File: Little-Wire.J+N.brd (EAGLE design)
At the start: 65 x 20 mm, 19 parts, among them J1 AVR_SPI_PRG_6PTH, J2 DCJ0202, X1 USB-A-H

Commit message: fixed stuff
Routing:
- net GND: track 14.2 -> 39.0 mm, vias 2 -> 1
- net VCC_HEADER: track 22.1 -> 11.1 mm
- net PIN4: track 27.2 -> 21.0 mm
- net PIN1: track 22.7 -> 24.1 mm
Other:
- board size 65 x 20 mm -> 65 x 22 mm
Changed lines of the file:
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@@
 <setting verticaltext="up"/>
 </settings>
-<grid distance="7" unitdist="mil" unit="mil" style="lines" multiple="1" display="yes" altdistance="0.025" altunitdist="inch" altunit="inch"/>
+<grid distance="0.5" unitdist="mm" unit="mm" style="lines" multiple="1" display="yes" altdistance="0.025" altunitdist="inch" altunit="inch"/>
 <layers>
 <layer number="1" name="Top" color="4" fill="1" visible="yes" active="yes"/>
@@
 <board>
 <plain>
-<wire x1="0" y1="0" x2="65" y2="0" width="0" layer="20"/>
-<wire x1="65" y1="0" x2="65" y2="20" width="0" layer="20"/>
+<wire x1="0" y1="-2" x2="65" y2="-2" width="0" layer="20"/>
+<wire x1="65" y1="-2" x2="65" y2="20" width="0" layer="20"/>
 <wire x1="65" y1="20" x2="0" y2="20" width="0" layer="20"/>
-<wire x1="0" y1="20" x2="0" y2="0" width="0" layer="20"/>
+<wire x1="0" y1="20" x2="0" y2="-2" width="0" layer="20"/>
 </plain>
 <attributes>
@@
 <autorouter>
 <pass name="Default">
-<param name="RoutingGrid" value="7mil"/>
+<param name="RoutingGrid" value="0.05mm"/>
 <param name="tpViaShape" value="round"/>
 <param name="PrefDir.1" value="|"/>
@@
 <contactref element="J2" pad="2"/>
 <contactref element="T2" pad="3"/>
-<polygon width="1.27" layer="16" isolate="0.3048" orphans="yes">
-<vertex x="0" y="19.9136"/>
-<vertex x="64.897" y="19.9136"/>
-<vertex x="64.897" y="0"/>
-<vertex x="0" y="0"/>
-</polygon>
-<polygon width="1.27" layer="1" isolate="0.3048" orphans="yes">
-<vertex x="0" y="19.9136"/>
-<vertex x="64.897" y="19.9136"/>
-<vertex x="64.897" y="0"/>
-<vertex x="0" y="0"/>
-</polygon>
 <wire x1="7.2898" y1="15.2908" x2="5.5118" y2="13.5128" width="0.254" layer="1"/>
 <wire x1="7.2898" y1="17.9578" x2="7.2898" y2="15.2908" width="0.254" layer="1"/>
 <wire x1="5.5118" y1="13.5128" x2="5.4" y2="13.5" width="0.254" layer="1"/>
 <wire x1="7.2898" y1="17.9578" x2="7.46" y2="18" width="0.254" layer="1"/>
-<wire x1="49.9618" y1="16.5354" x2="49.66485" y2="15.990384375" width="0.254" layer="1"/>
-<wire x1="47.2948" y1="17.0688" x2="47.539528125" y2="17.1811125" width="0.254" layer="1"/>
-<wire x1="52.0954" y1="17.0688" x2="52.539528125" y2="17.1811125" width="0.254" layer="1"/>
-<wire x1="46.9392" y1="17.2466" x2="47.539528125" y2="17.1811125" width="0.254" layer="1"/>
-<via x="52.451" y="17.4244" extent="1-16" drill="0.6096"/>
-<wire x1="40.7162" y1="11.3792" x2="39.4716" y2="11.3792" width="0.254" layer="1"/>
-<wire x1="39.4716" y1="11.3792" x2="39.3114" y2="11.4012" width="0.254" layer="1"/>
-<wire x1="40.7162" y1="11.3792" x2="40.3998" y2="11.831296875" width="0.254" layer="16"/>
-<wire x1="54.4068" y1="9.779" x2="54.4068" y2="9.3000125" width="0.254" layer="16"/>
-<wire x1="55.2958" y1="9.779" x2="55.2958" y2="9.29998125" width="0.254" layer="16"/>
-<wire x1="53.1622" y1="10.8458" x2="53.376184375" y2="11.188996875" width="0.254" layer="16"/>
-<wire x1="56.7182" y1="9.779" x2="56.7182" y2="9.29998125" width="0.254" layer="16"/>
-<via x="40.7162" y="11.3792" extent="1-16" drill="0.6096"/>
-<wire x1="55.8292" y1="9.6012" x2="55.8292" y2="9.29998125" width="0.254" layer="16"/>
-<wire x1="57.0738" y1="9.2456" x2="57.2925875" y2="8.691496875" width="0.254" layer="16"/>
-<wire x1="52.0954" y1="10.3124" x2="52.251821875" y2="10.723271875" width="0.254" layer="16"/>
-<wire x1="56.3626" y1="10.668" x2="56.923271875" y2="10.548175" width="0.254" layer="16"/>
-<wire x1="56.7182" y1="8.001" x2="56.337275" y2="7.602171875" width="0.254" layer="16"/>
-<wire x1="56.5404" y1="10.3124" x2="57.0740125" y2="10.351721875" width="0.254" layer="16"/>
-<wire x1="39.3114" y1="11.4012" x2="31.54" y2="12.92" width="0" layer="19" extent="1-1"/>
-<wire x1="23.19" y1="2.19" x2="31.54" y2="12.92" width="0" layer="19" extent="1-1"/>
-<wire x1="20" y1="2.46" x2="23.19" y2="2.19" width="0" layer="19" extent="1-1"/>
+<wire x1="20" y1="2.46" x2="23.19" y2="2.46" width="0.4064" layer="16"/>
+<wire x1="23.19" y1="2.46" x2="23.19" y2="2.19" width="0.4064" layer="16"/>
+<wire x1="23.19" y1="2.46" x2="27.559" y2="2.4892" width="0.254" layer="16"/>
+<wire x1="27.559" y1="2.4892" x2="27.559" y2="5.8674" width="0.254" layer="16"/>
+<wire x1="27.559" y1="5.8674" x2="32.1818" y2="5.8674" width="0.254" layer="16"/>
+<wire x1="32.1818" y1="5.8674" x2="32.1818" y2="10.8458" width="0.254" layer="16"/>
+<wire x1="32.1818" y1="10.8458" x2="31.54" y2="12.92" width="0.254" layer="16"/>
+<wire x1="38.4048" y1="12.446" x2="39.2938" y2="11.557" width="0.254" layer="1"/>
+<wire x1="38.4048" y1="13.335" x2="38.4048" y2="12.446" width="0.254" layer="1"/>
+<wire x1="36.9824" y1="14.7574" x2="38.4048" y2="13.335" width="0.254" layer="16"/>
+<wire x1="33.4264" y1="14.7574" x2="36.9824" y2="14.7574" width="0.254" layer="16"/>
+<wire x1="31.6484" y1="12.9794" x2="33.4264" y2="14.7574" width="0.254" layer="16"/>
+<wire x1="39.2938" y1="11.557" x2="39.3114" y2="11.4012" width="0.254" layer="1"/>
+<wire x1="31.6484" y1="12.9794" x2="31.54" y2="12.92" width="0.254" layer="16"/>
+<via x="38.4048" y="13.335" extent="1-16" drill="0.6096"/>
+<polygon width="0" layer="1" isolate="0.4064" orphans="yes">
+<vertex x="0" y="20"/>
+<vertex x="65" y="20"/>
+<vertex x="65" y="-2"/>
+<vertex x="0" y="-2"/>
+</polygon>
+<polygon width="0" layer="16" isolate="0.4064" orphans="yes">
+<vertex x="0" y="20"/>
+<vertex x="65" y="20"/>
+<vertex x="65" y="-2"/>
+<vertex x="0" y="-2"/>
+</polygon>
+<wire x1="7.4676" y1="18.8468" x2="7.4600125" y2="18.8468" width="0.254" layer="16"/>
+<wire x1="6.8" y1="14.8" x2="6.775646875" y2="14.824353125" width="0.254" layer="16"/>
 </signal>
 <signal name="N$1">
@@
 <wire x1="32.004" y1="11.557" x2="33.0708" y2="12.6238" width="0.254" layer="1"/>
 <wire x1="29.5148" y1="11.557" x2="32.004" y2="11.557" width="0.254" layer="1"/>
-<wire x1="29.5148" y1="6.0452" x2="29.5148" y2="10.4902" width="0.254" layer="1"/>
-<wire x1="29.5148" y1="10.4902" x2="29.5148" y2="11.557" width="0.254" layer="1"/>
-<wire x1="30.7594" y1="4.8006" x2="29.5148" y2="6.0452" width="0.254" layer="1"/>
+<wire x1="29.5148" y1="4.9784" x2="29.5148" y2="9.4234" width="0.254" layer="1"/>
+<wire x1="29.5148" y1="9.4234" x2="29.5148" y2="11.557" width="0.254" layer="1"/>
+<wire x1="30.7594" y1="4.8006" x2="29.5148" y2="4.9784" width="0.254" layer="1"/>
 <wire x1="34.671" y1="11.9126" x2="34.6886" y2="11.4012" width="0.254" layer="1"/>
 <wire x1="30.7594" y1="4.8006" x2="30.81" y2="4.73" width="0.254" layer="1"/>
 <wire x1="27.559" y1="16.5354" x2="28.9814" y2="17.9578" width="0.254" layer="1"/>
 <wire x1="27.559" y1="12.446" x2="27.559" y2="16.5354" width="0.254" layer="1"/>
-<wire x1="29.5148" y1="10.4902" x2="27.559" y2="12.446" width="0.254" layer="1"/>
+<wire x1="29.5148" y1="9.4234" x2="27.559" y2="12.446" width="0.254" layer="1"/>
 <wire x1="28.9814" y1="17.9578" x2="29" y2="18" width="0.254" layer="1"/>
 </signal>
@@
 <wire x1="34.4932" y1="10.8458" x2="34.4932" y2="13.335" width="0.254" layer="16"/>
 <wire x1="33.6042" y1="10.8458" x2="34.4932" y2="10.8458" width="0.254" layer="16"/>
-<wire x1="31.2928" y1="8.5344" x2="33.6042" y2="10.8458" width="0.254" layer="16"/>
-<wire x1="28.2702" y1="8.5344" x2="31.2928" y2="8.5344" width="0.254" layer="16"/>
-<wire x1="27.7368" y1="8.001" x2="28.2702" y2="8.5344" width="0.254" layer="16"/>
-<wire x1="27.7368" y1="2.3114" x2="27.7368" y2="8.001" width="0.254" layer="16"/>
-<wire x1="30.7594" y1="2.3114" x2="27.7368" y2="2.3114" width="0.254" layer="16"/>
+<wire x1="32.893" y1="8.5344" x2="33.6042" y2="10.8458" width="0.254" layer="16"/>
+<wire x1="32.893" y1="4.2672" x2="32.893" y2="8.5344" width="0.254" layer="16"/>
+<wire x1="30.7594" y1="2.3114" x2="32.893" y2="4.2672" width="0.254" layer="16"/>
 <wire x1="31.6484" y1="15.2908" x2="31.54" y2="15.46" width="0.254" layer="1"/>
 <wire x1="30.7594" y1="2.3114" x2="30.81" y2="2.19" width="0.254" layer="16"/>
@@
 <contactref element="JP1" pad="2"/>
 <contactref element="J1" pad="2"/>
-<wire x1="22.5806" y1="13.5128" x2="22.5806" y2="17.9578" width="0.254" layer="16"/>
-<wire x1="23.4696" y1="13.5128" x2="22.5806" y2="13.5128" width="0.254" layer="16"/>
-<wire x1="25.4254" y1="11.557" x2="23.4696" y2="13.5128" width="0.254" layer="16"/>
-<wire x1="32.004" y1="11.557" x2="25.4254" y2="11.557" width="0.254" layer="16"/>
-<wire x1="32.893" y1="12.446" x2="32.004" y2="11.557" width="0.254" layer="16"/>
-<wire x1="32.893" y1="16.002" x2="32.893" y2="12.446" width="0.254" layer="16"/>
-<wire x1="31.6484" y1="17.2466" x2="32.893" y2="16.002" width="0.254" layer="16"/>
+<wire x1="22.9362" y1="17.78" x2="22.5806" y2="17.9578" width="0.254" layer="16"/>
+<wire x1="23.8252" y1="17.78" x2="22.9362" y2="17.78" width="0.254" layer="16"/>
+<wire x1="27.0256" y1="16.7132" x2="23.8252" y2="17.78" width="0.254" layer="16"/>
+<wire x1="31.2928" y1="16.7132" x2="27.0256" y2="16.7132" width="0.254" layer="16"/>
+<wire x1="31.2928" y1="16.7132" x2="31.8262" y2="17.0688" width="0.254" layer="16"/>
+<wire x1="31.6484" y1="17.2466" x2="31.2928" y2="16.7132" width="0.254" layer="16"/>
 <wire x1="31.6484" y1="17.9578" x2="31.6484" y2="17.2466" width="0.254" layer="16"/>
 <wire x1="22.5806" y1="17.9578" x2="22.54" y2="18" width="0.254" layer="16"/>
@@
 <wire x1="55" y1="17" x2="55" y2="18" width="1.27" layer="16"/>
 </signal>
+<signal name="N$5">
+</signal>
 </signals>

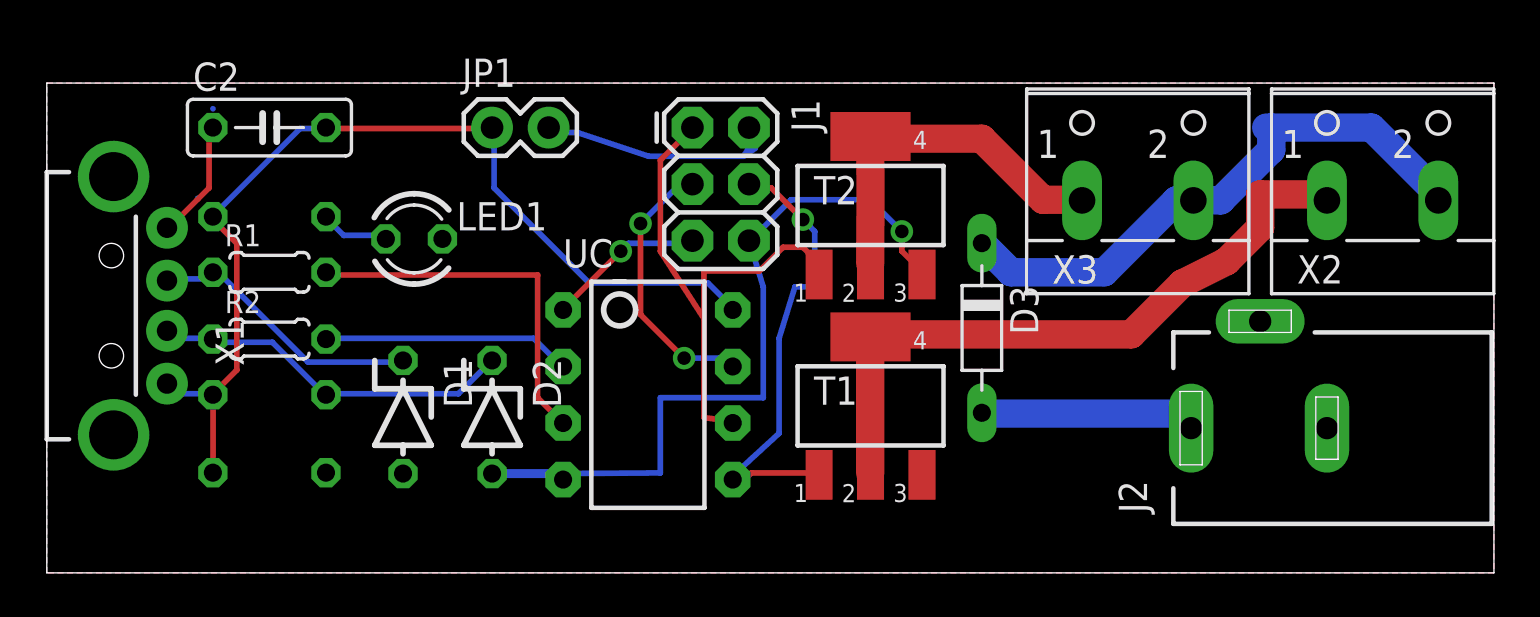
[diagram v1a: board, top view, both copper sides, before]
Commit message: fixed unrouted wires
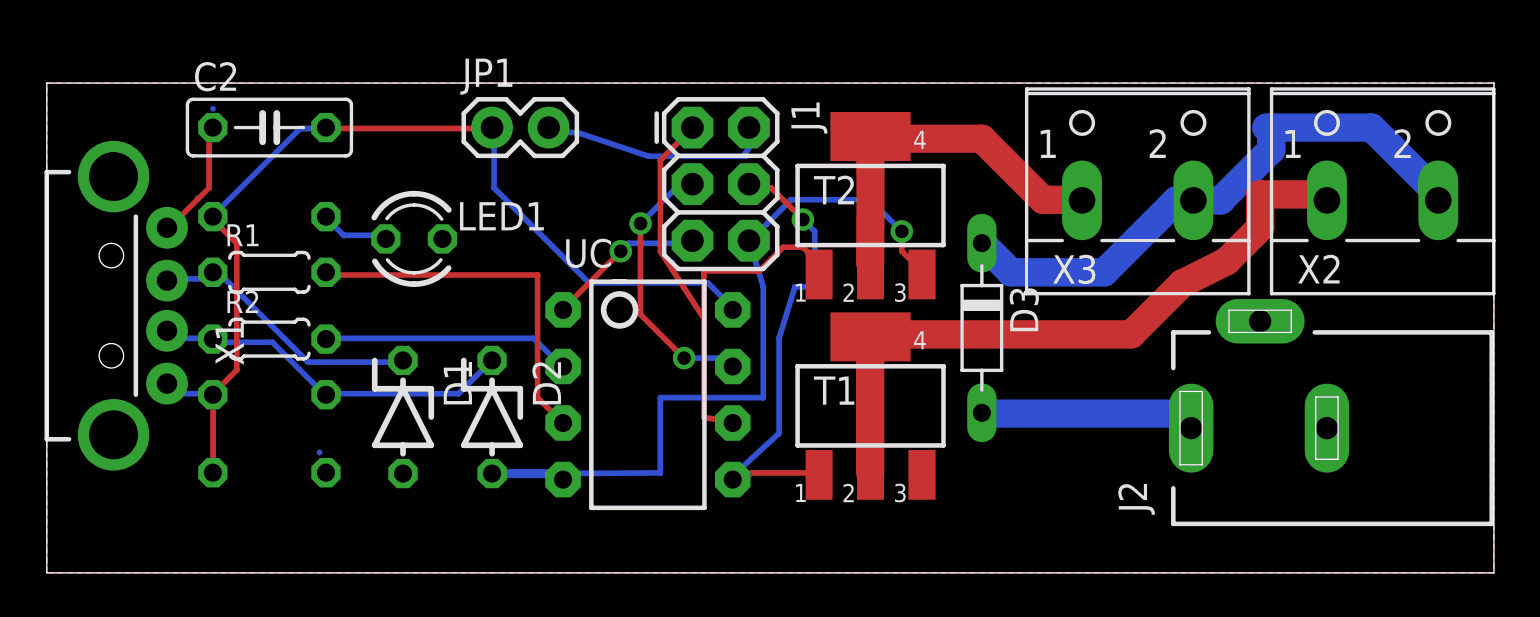
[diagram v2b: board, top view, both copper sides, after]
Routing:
- net GND: track 39.0 -> 40.3 mm
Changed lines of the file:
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@@
 <setting verticaltext="up"/>
 </settings>
-<grid distance="0.5" unitdist="mm" unit="mm" style="lines" multiple="1" display="yes" altdistance="0.025" altunitdist="inch" altunit="inch"/>
+<grid distance="0.1" unitdist="mm" unit="mm" style="lines" multiple="1" display="yes" altdistance="0.025" altunitdist="inch" altunit="inch"/>
 <layers>
 <layer number="1" name="Top" color="4" fill="1" visible="yes" active="yes"/>
@@
 <wire x1="7.4676" y1="18.8468" x2="7.4600125" y2="18.8468" width="0.254" layer="16"/>
 <wire x1="6.8" y1="14.8" x2="6.775646875" y2="14.824353125" width="0.254" layer="16"/>
+<wire x1="32.45" y1="16.45" x2="32.45191875" y2="16.451915625" width="0.254" layer="16"/>
+<wire x1="28.1" y1="11.95" x2="28.08308125" y2="11.933078125" width="0.254" layer="16"/>
+<wire x1="17.75" y1="13" x2="17.77" y2="13" width="0.254" layer="16"/>
+<wire x1="12.25" y1="3.4" x2="12.25" y2="3.414415625" width="0.254" layer="16"/>
+<wire x1="55.7" y1="9.3" x2="54.5" y2="9.3" width="0.254" layer="16"/>
 </signal>
 <signal name="N$1">
@@
 <wire x1="23.8252" y1="17.78" x2="22.9362" y2="17.78" width="0.254" layer="16"/>
 <wire x1="27.0256" y1="16.7132" x2="23.8252" y2="17.78" width="0.254" layer="16"/>
-<wire x1="31.2928" y1="16.7132" x2="27.0256" y2="16.7132" width="0.254" layer="16"/>
-<wire x1="31.2928" y1="16.7132" x2="31.8262" y2="17.0688" width="0.254" layer="16"/>
-<wire x1="31.6484" y1="17.2466" x2="31.2928" y2="16.7132" width="0.254" layer="16"/>
+<wire x1="31.6484" y1="17.2466" x2="31.396615625" y2="16.868921875" width="0.254" layer="16"/>
+<wire x1="31.396615625" y1="16.868921875" x2="31.2928" y2="16.7132" width="0.254" layer="16"/>
 <wire x1="31.6484" y1="17.9578" x2="31.6484" y2="17.2466" width="0.254" layer="16"/>
 <wire x1="22.5806" y1="17.9578" x2="22.54" y2="18" width="0.254" layer="16"/>
 <wire x1="31.6484" y1="17.9578" x2="31.54" y2="18" width="0.254" layer="16"/>
+<wire x1="27.0256" y1="16.7132" x2="31.396615625" y2="16.7132" width="0.254" layer="16"/>
+<wire x1="31.396615625" y1="16.7132" x2="31.396615625" y2="16.868921875" width="0.254" layer="16"/>
 </signal>
 <signal name="D+">
